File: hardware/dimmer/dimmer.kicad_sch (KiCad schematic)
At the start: 31 parts, among them J1 AC_IN_L_N, J2 AC_OUT_LOAD, J3 USB-C, Q1 BT138-600, Q2 MMBT3904, Q3 MMBT3904, SW1 BOOT, SW2 EN, U1 ESP32-WROOM-32, U2 TLP281-4, U3 MOC3021, U4 CP2102

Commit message: hardware: switch both boards to plug-in modules (ESP32 DevKit, TP4056)
Rework the schematic capture so every part maps to a hand-solderable module
or component you can buy from Robu / Robocraze / Quartz Components, per the
"hand-solder from modules" plan.

Both boards:
- Replace the bare ESP32-WROOM-32 + the entire onboard USB-serial subsystem
  (CP2102 QFN, board USB-C + CC resistors, two-transistor auto-reset, CP2102
  support caps/pull-ups, separate BOOT/EN buttons) with a plug-in ESP32
  DevKit V1 (30-pin) that carries its own USB bridge, micro-USB, auto-reset
  and BOOT/EN. Carrier now only routes 3V3/GND + the GPIOs it uses.

Remote:
- TP4056 bare SOP-8 -> TP4056 charge+protect module (charges via its own
  USB-C); external charge LEDs + PROG resistor removed (onboard the module).
  B+/B- -> LiPo, OUT+/OUT- -> ME6211 input.
- Tactile buttons -> 6mm THT footprint (SW_PUSH_6mm).
- Note: DevKit leaks in deep sleep, so battery life drops from months to
  days/weeks (accepted trade for simplicity; documented in CLAUDE.md).

parts.py: add ESP32_DevKit() and TP4056_module() symbols; drop bare CP2102 /
TP4056. Regenerated via gen_dimmer.py / gen_remote.py; validate.py reports no
floating pins on either board. Schematic files normalize back to the
generator's 20230121 format (KiCad 10 re-upgrades on open).
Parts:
- removed C3, C7: 100nF, Capacitor_SMD:C_0805_2012Metric, symbol Device:C
- removed C6: 1uF, Capacitor_SMD:C_0805_2012Metric, symbol Device:C
- removed J3: USB-C, Connector_USB:USB_C_Receptacle_HRO_TYPE-C-31-M-12, symbol Connector:USB_C_Receptacle_USB2.0_16P
- removed Q2, Q3: MMBT3904, Package_TO_SOT_SMD:SOT-23, symbol Transistor_BJT:MMBT3904
- removed R10, R9: 5.1k, Resistor_SMD:R_0805_2012Metric, symbol Device:R
- removed R6, R7, R8: 10k, Resistor_SMD:R_0805_2012Metric, symbol Device:R
- removed SW1: BOOT, Button_Switch_SMD:SW_SPST_PTS645, symbol Switch:SW_Push
- removed SW2: EN, Button_Switch_SMD:SW_SPST_PTS645, symbol Switch:SW_Push
- removed U1: ESP32-WROOM-32, RF_Module:ESP32-WROOM-32, symbol RF_Module:ESP32-WROOM-32
- removed U4: CP2102, Package_DFN_QFN:QFN-28-1EP_5x5mm_P0.5mm, symbol Interface_USB:CP2102
- added U1: ESP32-DevKitC-30, Module:ESP32-DevKitC, symbol Module:ESP32-DevKitC
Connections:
- net +3V3: now also U1.30 (3V3)
- net GATE_DRV: now also U1.8 (IO25)
- net GND: now also U1.13 (GND), U1.16 (GND)
- net ZC_DET: now also U1.4 (IO34)
- no-connect marks 40 -> 39
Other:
- note added: "=== ESP32 DevKit (plug-in module, flash over micro-USB) ==="
- note added: "Opto-TRIAC gate drive <- IO25"
- note added: "Programming: plug micro-USB into the ESP32 DevKit (onboard CP2102 + auto-reset). Do NOT power from mains and USB at the same time."
- note added: "Zero-cross detect -> IO34"
- note removed: "=== LOGIC 3V3 ==="
- note removed: "Opto-TRIAC gate drive <- GPIO25"
- note removed: "USB-Serial + auto-reset"
- note removed: "Zero-cross detect -> GPIO34"

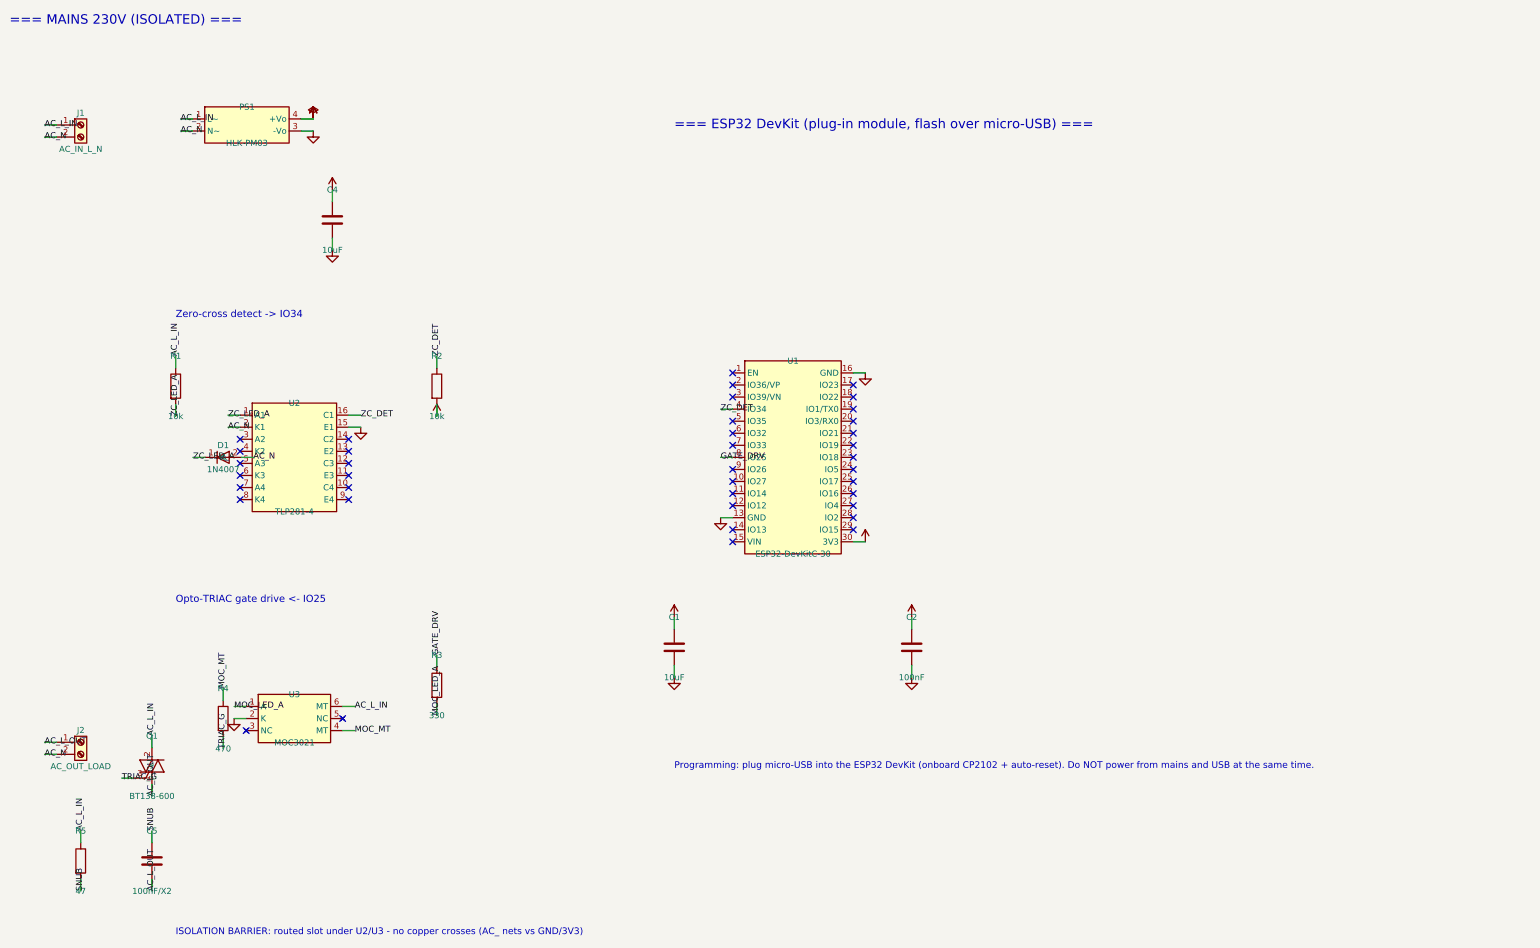
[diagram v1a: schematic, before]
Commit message: hardware: annotate both schematics with block boxes, headers, net legend
Add color-coded functional-block rectangles, colored block-title text,
and a signal/net-legend glossary to the dimmer and remote schematics for
readability. Also upgrades both .kicad_sch to KiCad 10 format. Netlist
connectivity verified unchanged on both boards (dimmer 12 nets, remote 8).
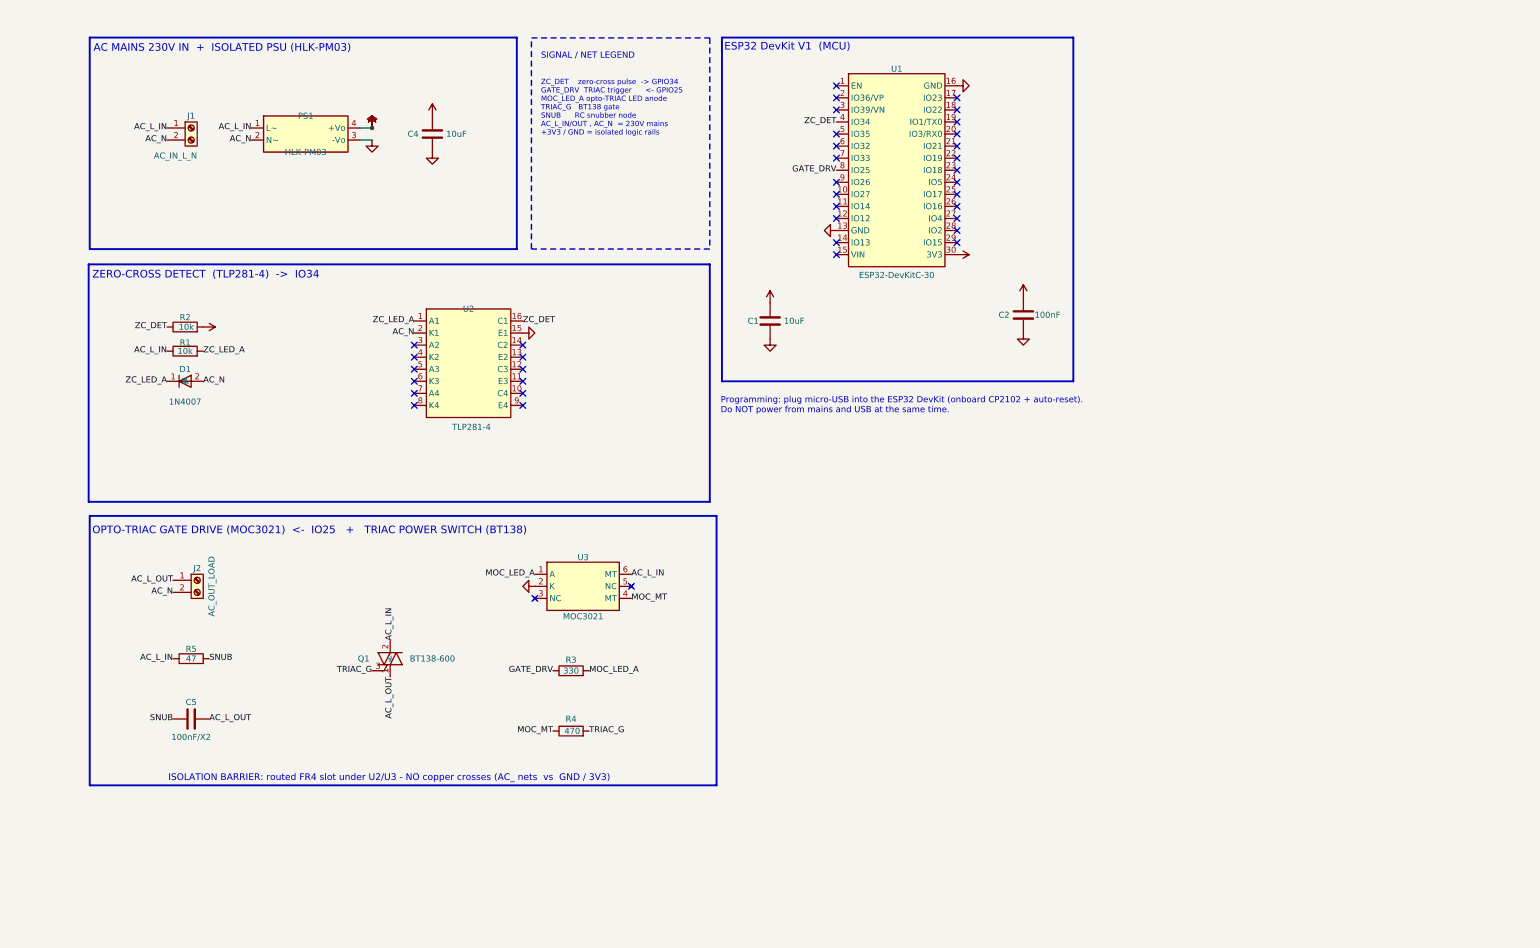
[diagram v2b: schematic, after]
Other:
- note added: "AC MAINS 230V IN + ISOLATED PSU (HLK-PM03)"
- note added: "ESP32 DevKit V1 (MCU)"
- note added: "ISOLATION BARRIER: routed FR4 slot under U2/U3 - NO copper crosses (AC_ nets vs GND / 3V3)"
- note added: "OPTO-TRIAC GATE DRIVE (MOC3021) <- IO25 + TRIAC POWER SWITCH (BT138)"
- note added: "SIGNAL / NET LEGEND"
- note added: "ZC_DET zero-cross pulse -> GPIO34 GATE_DRV TRIAC trigger <- GPIO25 MOC_LED_A opto-TRIAC LED anode TRIAC_G BT138 gate SNUB RC snubber node AC_L_IN/OUT , AC_N = 230V mains +3V3 / GND = isolated logic rails"
- note added: "ZERO-CROSS DETECT (TLP281-4) -> IO34"
- note removed: "=== ESP32 DevKit (plug-in module, flash over micro-USB) ==="
- note removed: "=== MAINS 230V (ISOLATED) ==="
- note removed: "ISOLATION BARRIER: routed slot under U2/U3 - no copper crosses (AC_ nets vs GND/3V3)"
- note removed: "Opto-TRIAC gate drive <- IO25"
- note removed: "Zero-cross detect -> IO34"
- moved on the sheet: C1, C2, C4, C5, D1, J1, J2, PS1, Q1, R1, R2, R3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

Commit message: hardware(remote): first-pass PCB layout (placement + netlist + outline)
Bootstraps the remote board PCB from the captured schematic.

- gen_remote_pcb.py: kiutils-based PCB generator. Loads real KiCad footprints,
  places every part in functional groups (charge/power on the left, DevKit on
  the right, three button stacks along the bottom), assigns the full schematic
  netlist to the pads, and draws the Edge.Cuts outline (78x60mm). Includes a
  pad-bbox overlap self-check (no GUI DRC here). Traces + GND pour are the next
  pass. Netlist is taken from a freshly generated kiutils-native schematic, not
  the committed file, because KiCad re-saved the schematic into a newer format
  that kiutils under-parses.

- Custom footprint IoT_AC_Dimmer:ESP32-DevKitC-30 (30-pin DevKit V1, two 1x15
  rows at 0.9in). Registered via project fp-lib-tables. Schematic footprint
  field updated to reference it (was a non-existent placeholder).

- gen_remote.py: REMOTE_SCH_OUT env override so tooling can emit a scratch
  schematic without touching the committed one.

Verified: 17 footprints, 8 nets, 48 netted pads, no overlaps, in-outline.

NOTE (first pass to verify in KiCad): the DevKit footprint row spacing (0.9in)
and the TP4056-module pad mapping should be checked against the physical parts
before fab; routing and the GND pour are still to do.
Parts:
- U1: footprint Module:ESP32-DevKitC -> IoT_AC_Dimmer:ESP32-DevKitC-30; symbol Module:ESP32-DevKitC -> IoT_AC_Dimmer:ESP32-DevKitC-30
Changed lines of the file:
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@@
 	)
 	(symbol
-		(lib_id "Module:ESP32-DevKitC")
+		(lib_id "IoT_AC_Dimmer:ESP32-DevKitC-30")
 		(at 196.85 49.53 0)
 		(unit 1)
@@
 			)
 		)
-		(property "Footprint" "Module:ESP32-DevKitC"
+		(property "Footprint" "IoT_AC_Dimmer:ESP32-DevKitC-30"
 			(at 196.85 49.53 0)
 			(hide yes)
